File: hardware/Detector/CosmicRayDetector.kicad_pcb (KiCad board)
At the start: 2 copper layers, 89.9 x 82.6 mm, 129 parts, among them J1 USB_B_Micro, J10 Conn_02x02_Odd_Even, J11 Conn_02x02_Odd_Even, J12 Conn_02x02_Odd_Even, J13 Conn_02x02_Odd_Even, J14 Conn_02x02_Odd_Even, J15 Conn_02x02_Odd_Even, J16 Conn_02x02_Odd_Even, J17 Conn_02x02_Odd_Even, J2 Conn_02x02_Odd_Even, J3 Conn_02x02_Odd_Even, J4 Conn_02x02_Odd_Even, J5 Conn_02x02_Odd_Even, J51 Conn_02x05_Counter_Clockwise, J52 Conn_01x04, J6 Conn_02x02_Odd_Even, J7 Conn_02x02_Odd_Even, J8 Conn_02x02_Odd_Even, J9 Conn_02x02_Odd_Even, Q31 BC859, Q32 Q_NMOS_GDS, U1 STM32F030K6Tx, U2 HEF4093B, U3 LCD_I2C, U31 MC34063AD

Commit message: iunified names of files
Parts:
- GM1, GM2, GM3, GM4, GM5, GM6, GM7, GM8: footprint MuonDetector:GeigerTube -> CosmicRayDetector:GeigerTube
- U3: footprint MuonDetector:LCD_I2C -> CosmicRayDetector:LCD_I2C

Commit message: cleanup
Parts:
- moved H2 128.6 mm to (7.62, 78.7)
- moved H1 127.0 mm to (81.3, 78.7)
- moved C2 125.7 mm to (40.8, 63.8)
- moved C35 125.7 mm to (43.4, 63.3)
- moved D32 125.7 mm to (25.1, 61.1)
- moved Q31 125.7 mm to (25.1, 65.2)
- moved C31 125.7 mm to (25.9, 73.8)
- moved C32 125.7 mm to (21.3, 80.3)
- moved C39 125.7 mm to (20.4, 63.1)
- moved GM1 125.7 mm to (13.3, 66.9)
- moved GM2 125.7 mm to (77.2, 66.5)
- moved GM3 125.7 mm to (13.3, 55.9)
- moved GM4 125.7 mm to (77.2, 55.5)
- moved GM5 125.7 mm to (13.3, 44.9)
- moved GM6 125.7 mm to (77.2, 44.5)
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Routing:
- net GND: track 10.9 -> 23.4 mm
- net COL2: track 134.6 -> 128.1 mm
- net GM4: track 64.9 -> 60.3 mm
- net Net-(C24-Pad1): track 52.8 -> 49.2 mm
- net GM1: track 71.9 -> 68.4 mm
- net ROW1: track 29.3 -> 27.5 mm
- net VCC_5V: track 262.8 -> 264.5 mm, vias 0 -> 1
- net ROW0: track 25.3 -> 23.8 mm
- net Net-(TP8-Pad1): track 4.54 -> 3.03 mm
- net /DataAcquisition/SWCLK: track 35.9 -> 34.5 mm
- net Net-(R59-Pad1): track 6.45 -> 5.54 mm
- net Net-(C21-Pad1): track 45.7 -> 46.6 mm
- net COL1: track 68.0 -> 67.3 mm
- net Net-(TP7-Pad1): track 2.70 -> 3.22 mm
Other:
- board size 89.9 x 82.6 mm -> 88.9 x 78.8 mm

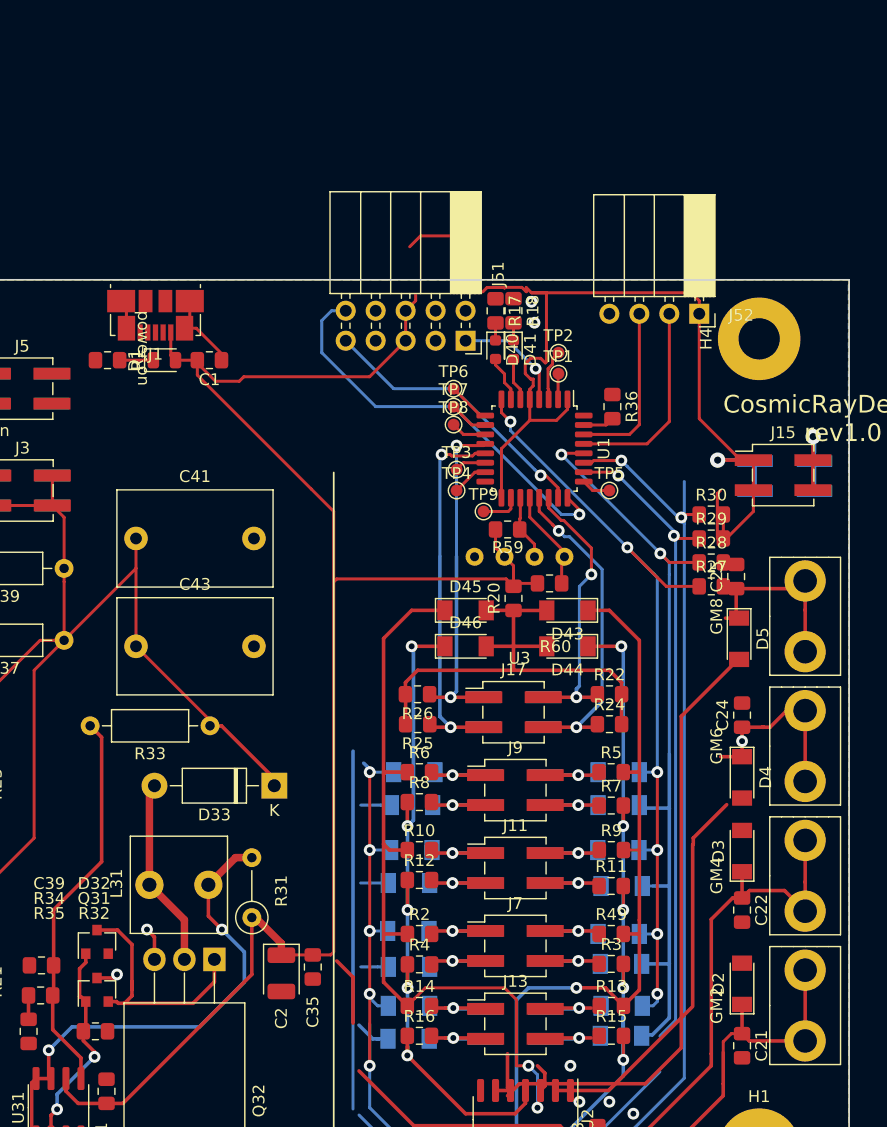
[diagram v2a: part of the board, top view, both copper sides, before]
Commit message: draft of board connector
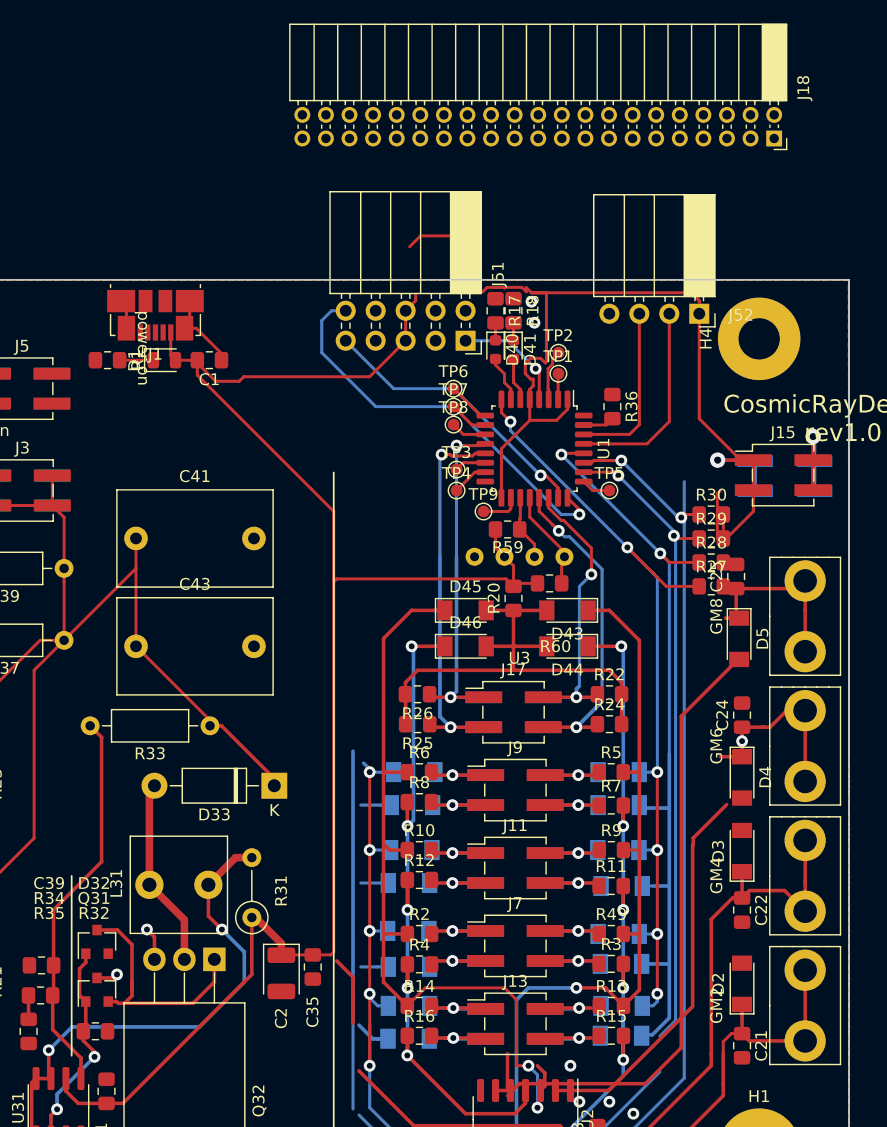
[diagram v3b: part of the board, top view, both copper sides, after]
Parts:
- added J18: Conn_02x20_Counter_Clockwise, Connector_PinSocket_2.00mm:PinSocket_2x21_P2.00mm_Horizontal, F.Cu at (82.5, -6.99)

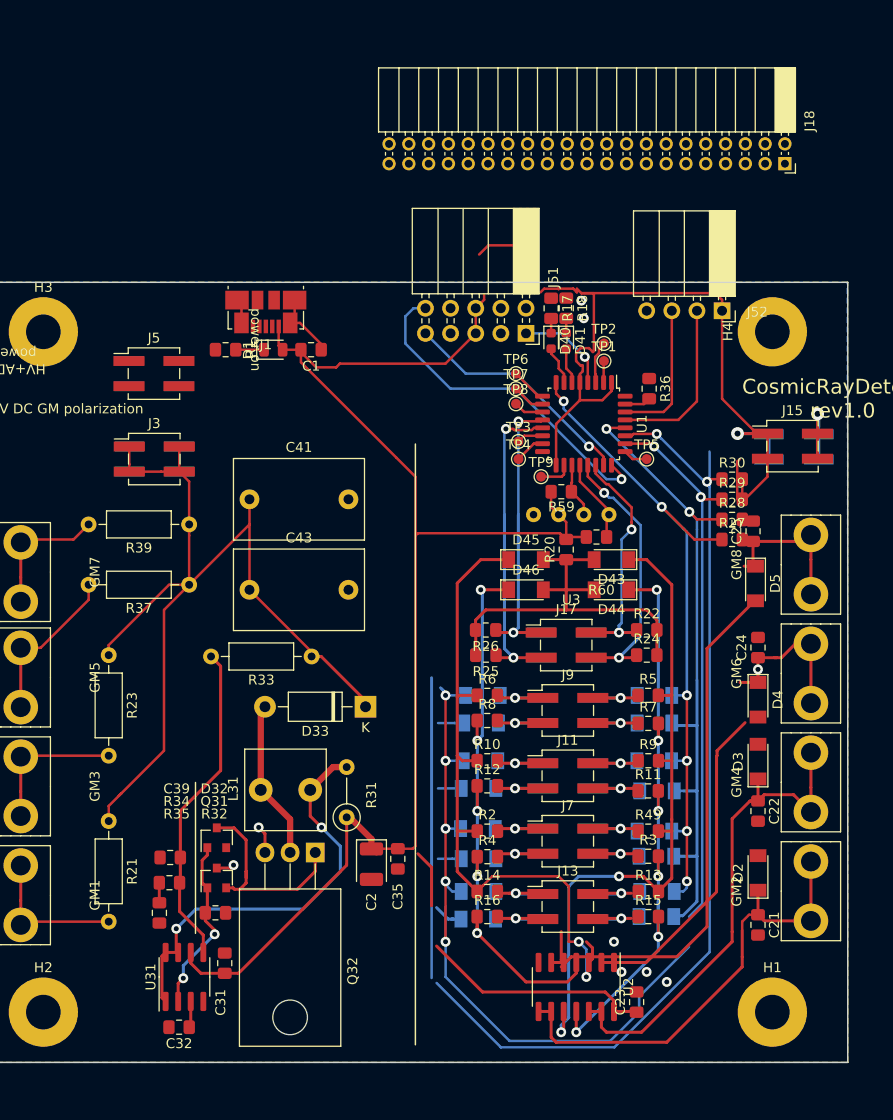
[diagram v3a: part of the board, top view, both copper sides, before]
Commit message: draft of version without expensive connectors
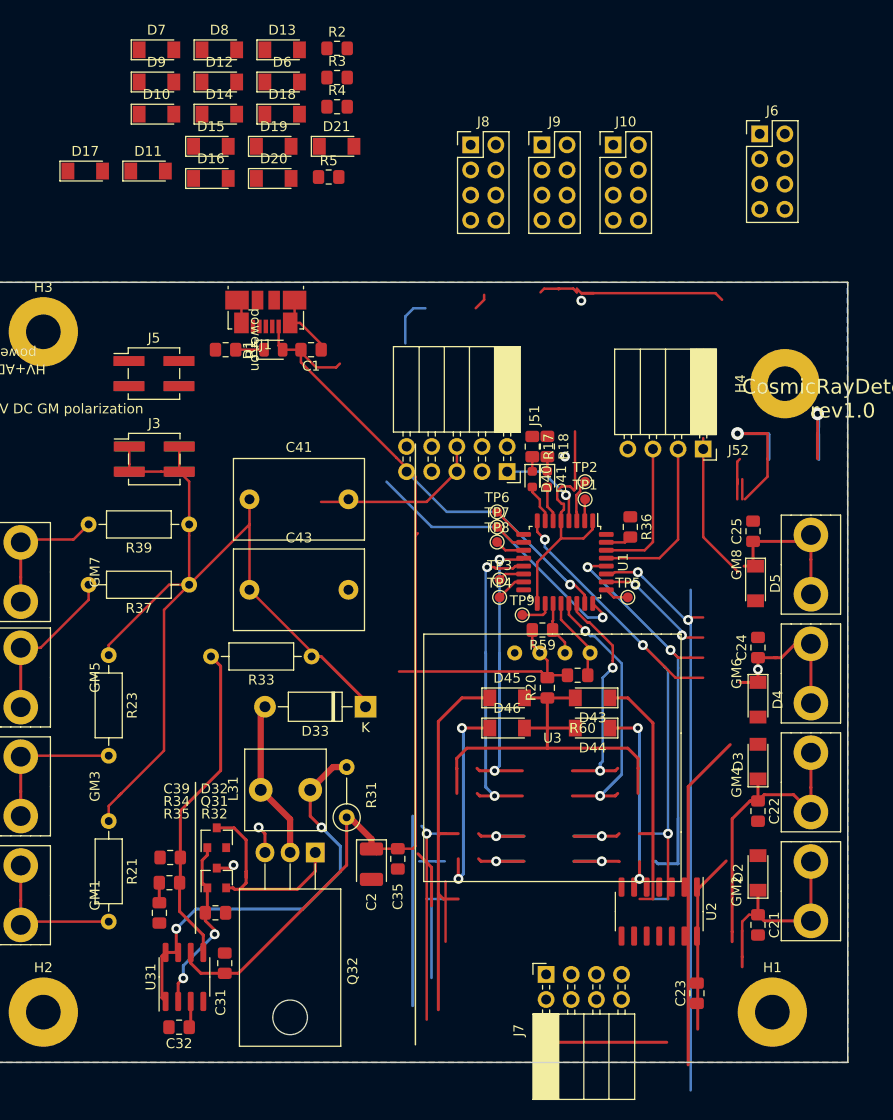
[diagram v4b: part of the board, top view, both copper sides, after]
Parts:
- removed J11, J13, J15, J17: Conn_02x02_Odd_Even, Connector_PinHeader_2.54mm:PinHeader_2x02_P2.54mm_Vertical_SMD
- removed J12, J14, J16: Conn_02x02_Odd_Even, Connector_PinSocket_2.54mm:PinSocket_2x02_P2.54mm_Vertical_SMD
- removed J18: Conn_02x20_Counter_Clockwise, Connector_PinSocket_2.00mm:PinSocket_2x21_P2.00mm_Horizontal
- removed R10, R11, R12, R13, R14, R15, R16, R22, R24, R25, R26, R49, R6, R7, R8, R9: R, Resistor_SMD:R_0805_2012Metric_Pad1.15x1.40mm_HandSolder
- removed R27, R28, R29, R30: 680R, Resistor_SMD:R_0805_2012Metric_Pad1.15x1.40mm_HandSolder
- D10, D11, D12, D13, D14, D15, D16, D17, D18, D19, D20, D21, D6, D7, D8, D9: moved to F.Cu
- J10, J6, J8: value Conn_02x02_Odd_Even -> Conn_02x04_Odd_Even; footprint Connector_PinSocket_2.54mm:PinSocket_2x02_P2.54mm_Vertical_SMD -> Connector_PinHeader_2.54mm:PinHeader_2x04_P2.54mm_Vertical; moved to F.Cu
- J7: value Conn_02x02_Odd_Even -> Conn_02x04_Odd_Even; footprint Connector_PinHeader_2.54mm:PinHeader_2x02_P2.54mm_Vertical_SMD -> Connector_PinSocket_2.54mm:PinSocket_2x04_P2.54mm_Horizontal
- J9: value Conn_02x02_Odd_Even -> Conn_02x04_Odd_Even; footprint Connector_PinHeader_2.54mm:PinHeader_2x02_P2.54mm_Vertical_SMD -> Connector_PinHeader_2.54mm:PinHeader_2x04_P2.54mm_Vertical
- R2, R3, R4, R5: value R -> 680R
- moved D9 96.2 mm to (19.1, -15.2)
- moved D13 95.4 mm to (31.8, -18.5)
- moved D10 90.4 mm to (19.1, -12.0)
- moved R3 84.7 mm to (37.3, -15.7)
- moved D6 84.5 mm to (31.8, -15.2)
- moved D8 84.2 mm to (25.4, -18.5)
- moved D12 84.2 mm to (25.4, -15.2)
- moved D17 82.9 mm to (11.8, -6.24), turned to 0 degrees
- moved D7 82.4 mm to (19.1, -18.5)
- moved R2 80.5 mm to (37.3, -18.6)
- moved D21 79.4 mm to (37.2, -8.74), turned to 0 degrees
- moved D18 77.8 mm to (31.8, -12.0), turned to 0 degrees
- moved R4 77.3 mm to (37.3, -12.7)
- moved D14 76.8 mm to (25.4, -12.0), turned to 0 degrees
- moved D11 75.7 mm to (18.2, -6.24)
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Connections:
- J10 pad 1: INT23 -> GND
- J10 pad 2: INT21 -> INT34
- J10 pad 3: INT24 -> GND
- J10 pad 4: INT22 -> INT33
- J6 pad 1: INT03 -> GND
- J6 pad 2: INT01 -> INT04
- J6 pad 3: INT04 -> GND
- J6 pad 4: INT02 -> INT03
- J7 pad 1: INT03 -> GND
- J7 pad 2: INT01 -> GM4
- J7 pad 3: INT04 -> GND
- J7 pad 4: INT02 -> GM3
- J8 pad 1: INT13 -> GND
- J8 pad 2: INT11 -> INT13
- J8 pad 3: INT14 -> GND
- J8 pad 4: INT12 -> INT14
- J9 pad 1: INT13 -> GND
- J9 pad 2: INT11 -> INT24
- J9 pad 3: INT14 -> GND
- J9 pad 4: INT12 -> INT23
- R2 pad 1: GM3 -> COL0
- R2 pad 2: INT03 -> VCC_5V
- R3 pad 1: INT02 -> COL1
- R3 pad 2: GM2 -> VCC_5V
- R4 pad 1: GM4 -> COL2
- R4 pad 2: INT04 -> VCC_5V
- R5 pad 1: INT11 -> COL3
- R5 pad 2: GM1 -> VCC_5V
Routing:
- net COL2: track 128.1 -> 41.9 mm, vias 7 -> 3
- net Net-(C25-Pad1): track 70.4 -> 15.4 mm
- net GM2: track 64.5 -> 19.9 mm, vias 6 -> 2
- net GM1: track 68.4 -> 25.9 mm, vias 2 -> 0
- net COL3: track 138.8 -> 96.6 mm
- net GM4: track 60.3 -> 20.4 mm, vias 5 -> 2
- net GND: track 23.4 -> 57.5 mm, vias 8 -> 5
- net VCC_5V: track 264.5 -> 234.1 mm
- net GM3: track 67.8 -> 39.6 mm, vias 2 -> 0
- net COL1: track 67.3 -> 41.9 mm
- net Net-(C22-Pad1): track 50.4 -> 30.3 mm
- net COL0: track 70.2 -> 54.4 mm, vias 6 -> 3
- net Net-(C21-Pad1): track 46.6 -> 31.2 mm
- net Net-(C24-Pad1): track 49.2 -> 34.6 mm
- net INT34: track 8.25 -> 0.00 mm, vias 1 -> 0
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
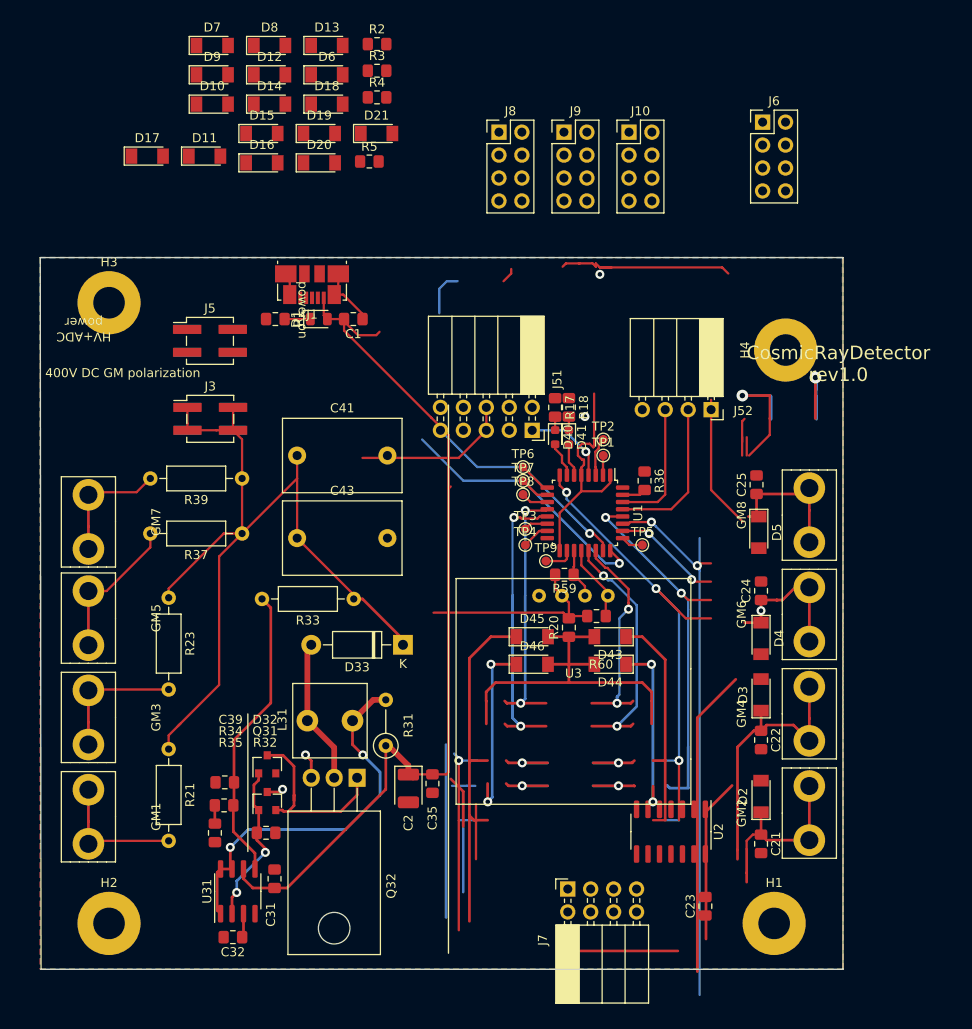
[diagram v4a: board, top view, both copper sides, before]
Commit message: fixed labels, changed board size
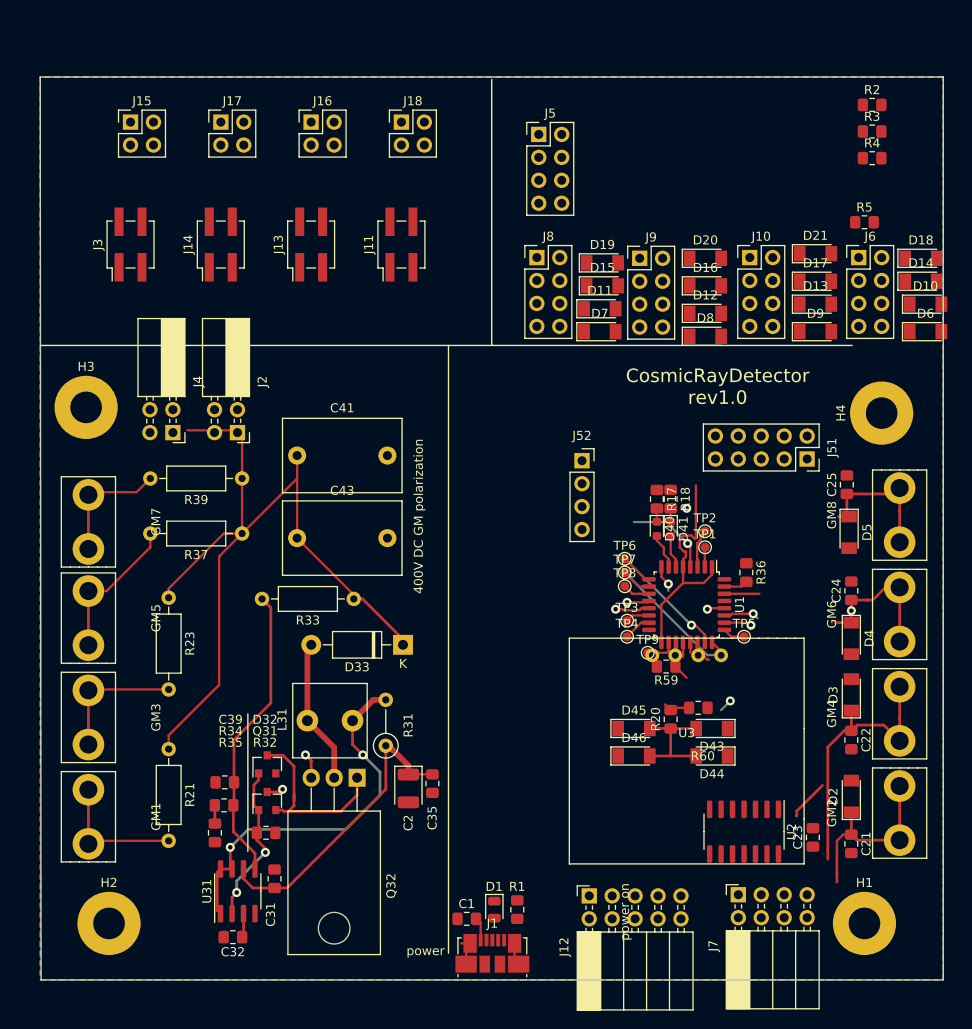
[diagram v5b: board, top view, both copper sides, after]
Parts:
- added J11: Conn_02x02_Odd_Even, Connector_PinHeader_2.54mm:PinHeader_2x02_P2.54mm_Vertical_SMD, F.Cu at (40.0, 3.56)
- added J12: Conn_02x04_Odd_Even, Connector_PinSocket_2.54mm:PinSocket_2x05_P2.54mm_Horizontal, F.Cu at (60.8, 75.7)
- added J13: Conn_02x02_Odd_Even, Connector_PinHeader_2.54mm:PinHeader_2x02_P2.54mm_Vertical_SMD, F.Cu at (30.0, 3.56)
- added J14: Conn_02x02_Odd_Even, Connector_PinHeader_2.54mm:PinHeader_2x02_P2.54mm_Vertical_SMD, F.Cu at (20.0, 3.56)
- added J15: Conn_02x02_Odd_Even, Connector_PinHeader_2.54mm:PinHeader_2x02_P2.54mm_Vertical, F.Cu at (10.0, -10.0)
- added J16: Conn_02x02_Odd_Even, Connector_PinHeader_2.54mm:PinHeader_2x02_P2.54mm_Vertical, F.Cu at (30.0, -10.0)
- added J17: Conn_02x02_Odd_Even, Connector_PinHeader_2.54mm:PinHeader_2x02_P2.54mm_Vertical, F.Cu at (20.0, -10.0)
- added J18: Conn_02x02_Odd_Even, Connector_PinHeader_2.54mm:PinHeader_2x02_P2.54mm_Vertical, F.Cu at (40.0, -10.0)
- J2, J4: footprint Connector_PinSocket_2.54mm:PinSocket_2x02_P2.54mm_Vertical_SMD -> Connector_PinSocket_2.54mm:PinSocket_2x02_P2.54mm_Horizontal; moved to F.Cu
- J5: value Conn_02x02_Odd_Even -> Conn_02x04_Odd_Even; footprint Connector_PinHeader_2.54mm:PinHeader_2x02_P2.54mm_Vertical_SMD -> Connector_PinHeader_2.54mm:PinHeader_2x04_P2.54mm_Vertical
- J51: footprint Connector_PinSocket_2.54mm:PinSocket_2x05_P2.54mm_Horizontal -> Connector_PinSocket_2.54mm:PinSocket_2x05_P2.54mm_Vertical
- J52: footprint Connector_PinSocket_2.54mm:PinSocket_1x04_P2.54mm_Horizontal -> Connector_PinSocket_2.54mm:PinSocket_1x04_P2.54mm_Vertical
- moved D10 82.0 mm to (98.0, 10.2)
- moved J1 76.7 mm to (50.1, 82.1), turned to 0 degrees
- moved D17 75.3 mm to (85.9, 7.62)
- moved D14 74.8 mm to (97.5, 7.62)
- moved D9 72.6 mm to (85.9, 13.2)
- moved D6 72.1 mm to (98.0, 13.2)
- moved R1 70.7 mm to (52.8, 77.2), turned to 270 degrees
- moved D1 68.2 mm to (50.3, 77.2), turned to 270 degrees
- moved D18 68.0 mm to (97.5, 5.08)
- moved C1 67.6 mm to (47.2, 78.2), turned to 0 degrees
- moved D13 61.2 mm to (85.9, 10.2)
- moved D8 58.0 mm to (73.7, 13.7)
- moved R2 55.2 mm to (92.1, -11.9)
- moved R3 55.2 mm to (92.1, -8.96)
- moved R4 55.2 mm to (92.1, -6.01)
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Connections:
- D10 pad 2: COL1 -> /BoardConnector/COL1_LOCAL
- D11 pad 2: COL1 -> /BoardConnector/COL1_LOCAL
- D12 pad 2: COL1 -> /BoardConnector/COL1_LOCAL
- D13 pad 2: COL1 -> /BoardConnector/COL1_LOCAL
- D14 pad 2: COL2 -> /BoardConnector/COL2_LOCAL
- D15 pad 2: COL2 -> /BoardConnector/COL2_LOCAL
- D16 pad 2: COL2 -> /BoardConnector/COL2_LOCAL
- D17 pad 2: COL2 -> /BoardConnector/COL2_LOCAL
- D18 pad 2: COL3 -> /BoardConnector/COL3_LOCAL
- D19 pad 2: COL3 -> /BoardConnector/COL3_LOCAL
- D20 pad 2: COL3 -> /BoardConnector/COL3_LOCAL
- D21 pad 2: COL3 -> /BoardConnector/COL3_LOCAL
- D6 pad 2: COL0 -> /BoardConnector/COL0_LOCAL
- D7 pad 2: COL0 -> /BoardConnector/COL0_LOCAL
- D8 pad 2: COL0 -> /BoardConnector/COL0_LOCAL
- D9 pad 2: COL0 -> /BoardConnector/COL0_LOCAL
- J10 pad 7: ROW3 -> /BoardConnector/ROW3_LOCAL
- J5 pad 1: GND -> COL0
- J5 pad 2: GND -> ROW0
- J5 pad 3: GND -> COL1
- J5 pad 4: GND -> ROW1
- J6 pad 7: ROW0 -> /BoardConnector/ROW0_LOCAL
- J8 pad 2: INT13 -> INT14
- J8 pad 4: INT14 -> INT13
- J8 pad 7: ROW1 -> /BoardConnector/ROW1_LOCAL
- J9 pad 7: ROW2 -> /BoardConnector/ROW2_LOCAL
- R2 pad 1: COL0 -> /BoardConnector/COL0_LOCAL
- R3 pad 1: COL1 -> /BoardConnector/COL1_LOCAL
- R4 pad 1: COL2 -> /BoardConnector/COL2_LOCAL
- R5 pad 1: COL3 -> /BoardConnector/COL3_LOCAL
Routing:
- net VCC_5V: track 234.1 -> 65.3 mm, vias 1 -> 0
- net COL3: track 96.6 -> 3.97 mm, vias 2 -> 1
- net COL0: track 54.4 -> 2.97 mm, vias 3 -> 1
- net GND: track 57.5 -> 10.6 mm, vias 5 -> 3
- net COL1: track 41.9 -> 1.93 mm, vias 2 -> 1
- net GM3: track 39.6 -> 0.00 mm
- net COL2: track 41.9 -> 3.10 mm, vias 3 -> 1
- net Net-(D43-Pad2): track 40.6 -> 12.3 mm
- net ROW2: track 32.1 -> 4.05 mm, vias 2 -> 1
- net ROW1: track 27.5 -> 1.14 mm, vias 2 -> 0
- net ROW3: track 28.7 -> 2.50 mm, vias 2 -> 1
- net GM1: track 25.9 -> 0.00 mm
- net GM4: track 20.4 -> 0.00 mm, vias 2 -> 0
- net GM2: track 19.9 -> 0.00 mm, vias 2 -> 0
- net ROW0: track 23.8 -> 4.01 mm, vias 2 -> 1
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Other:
- board size 88.9 x 78.8 mm -> 100 x 100 mm
- board text added: "power"
- board text removed: "HV+ADC power"
